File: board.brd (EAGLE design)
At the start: 50 x 70 mm, 25 parts

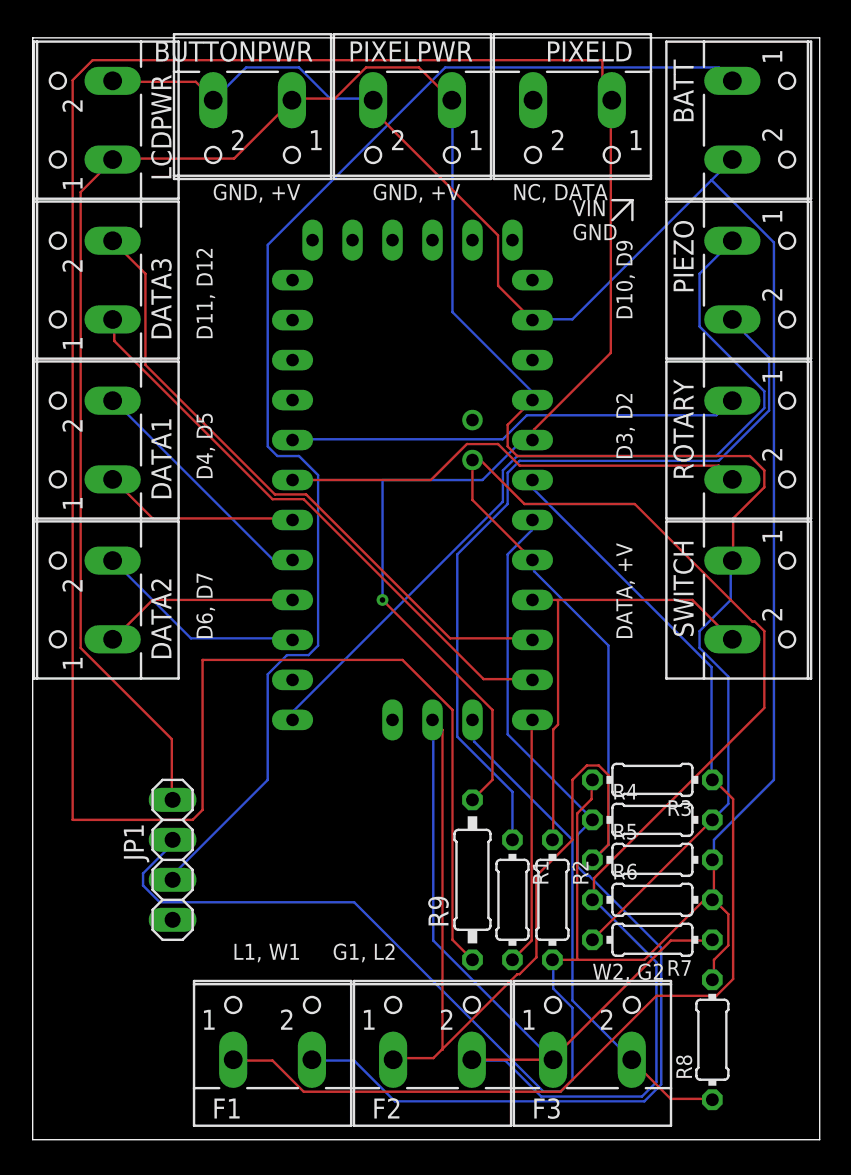
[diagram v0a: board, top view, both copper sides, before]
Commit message: New Molex version of PCB
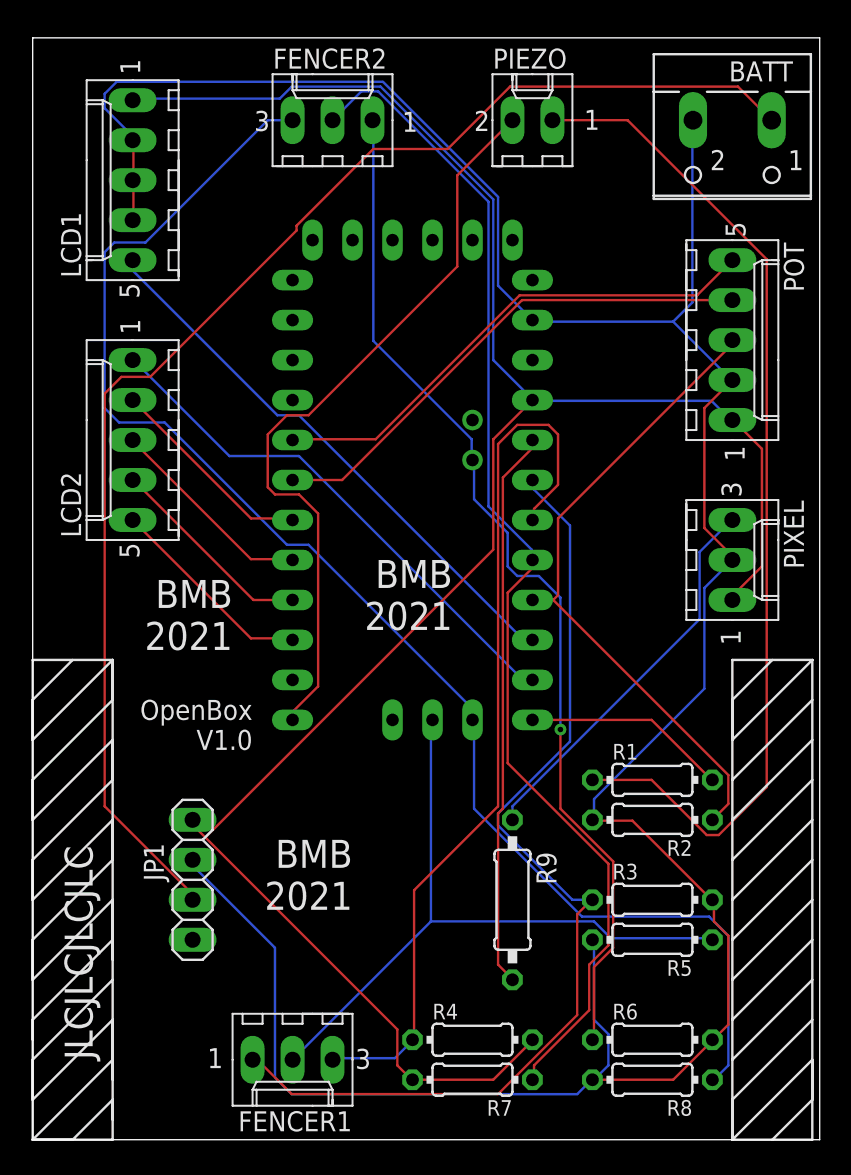
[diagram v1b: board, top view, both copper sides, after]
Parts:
- removed BUTTONPWR, DATA1, DATA2, DATA3, F1, F2, F3, LCDPWR, PIXELD, PIXELPWR, ROTARY, SWITCH: (no value), con-wago-500:W237-102
- added FENCER1, FENCER2, PIXEL: 22-27-2031-03, EP_molex_6410_7395:6410-03
- added LCD1, LCD2, POT: 22-27-2051-05, EP_molex_6410_7395:6410-05
- PIEZO: value (none) -> 22-27-2021-02; device con-wago-500:W237-102 -> EP_molex_6410_7395:6410-02
- moved R4 18.1 mm to (27.9, 6.35)
- moved PIEZO 17.3 mm to (31.8, 64.8), turned to 0 degrees
- moved R7 14.5 mm to (27.9, 3.81)
- moved R1 11.7 mm to (39.4, 22.9), turned to 0 degrees
- moved R6 8.89 mm to (39.4, 6.35)
- moved R2 8.13 mm to (39.4, 20.3), turned to 180 degrees
- moved R3 7.62 mm to (39.4, 15.2), turned to 0 degrees
- moved R5 5.08 mm to (39.4, 12.7), turned to 180 degrees
- moved R8 4.58 mm to (39.4, 3.81), turned to 180 degrees
- moved R9 2.84 mm to (30.5, 15.2), turned to 270 degrees
- moved JP1 1.80 mm to (10.2, 16.5)
- moved BATT 1.80 mm to (44.5, 63.5), turned to 180 degrees
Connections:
- new net N$24: FENCER2.2, R7.1, U$1.A3
- net N$1: now also LCD1.1, PIXEL.1, POT.1; no longer BUTTONPWR.1, LCDPWR.1, PIXELPWR.1, SWITCH.1
- net N$10: now also PIEZO.2; no longer PIEZO.1
- net N$11: now also PIEZO.1; no longer PIEZO.2
- net N$13: now also POT.5; no longer ROTARY.1
- net N$14: now also POT.4; no longer ROTARY.2
- net N$15: now also FENCER1.1; no longer F1.1
- net N$16: now also POT.3; no longer SWITCH.2
- net N$18: now also FENCER1.3; no longer F1.2
- net N$19: now also FENCER1.2; no longer F2.1
- net N$2: now also LCD1.2, LCD1.3, LCD1.4, PIXEL.2, POT.2; no longer BUTTONPWR.2, LCDPWR.2, PIXELPWR.2
- net N$20: now also FENCER2.1; no longer F2.2, F3.1, R7.1, U$1.A3
- net N$22: now also FENCER2.3; no longer F3.2
- net N$23: now also PIXEL.3; no longer PIXELD.1
- net N$4: now also LCD2.4; no longer DATA2.1
- net N$5: now also LCD2.1; no longer DATA3.1
- net N$6: now also LCD1.5; no longer DATA3.2
- net N$7: now also LCD2.2; no longer DATA1.1
- net N$8: now also LCD2.3; no longer DATA1.2
- net N$9: now also LCD2.5; no longer DATA2.2
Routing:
- net N$23: track 135.9 -> 24.9 mm
- net N$24: track 0.00 -> 75.9 mm
- net N$22: track 32.0 -> 92.2 mm
- net N$20: track 122.2 -> 66.2 mm, vias 0 -> 1
- net N$19: track 75.4 -> 43.7 mm
- net N$17: track 57.9 -> 35.6 mm, vias 1 -> 0
- net N$11: track 51.1 -> 64.6 mm
- net N$1: track 146.3 -> 133.7 mm
- net N$16: track 29.1 -> 41.6 mm
- net N$18: track 65.2 -> 56.5 mm
- net N$15: track 72.7 -> 64.2 mm
- net N$6: track 40.6 -> 35.8 mm
- net N$10: track 52.9 -> 48.3 mm
- net N$3: track 81.6 -> 86.1 mm
- net N$2: track 177.4 -> 181.7 mm
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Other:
- board text added: "BMB 2021"
- board text added: "JLCJLCJLCJLC"
- board text added: "OpenBox V1.0"
- board text removed: "D10, D9"
- board text removed: "D11, D12"
- board text removed: "D3, D2"
- board text removed: "D4, D5"
- board text removed: "D6, D7"
- board text removed: "DATA, +V"
- board text removed: "G1, L2"
- board text removed: "GND, +V"
- board text removed: "L1, W1"
- board text removed: "NC, DATA"
- board text removed: "VIN GND"
- board text removed: "W2, G2"
